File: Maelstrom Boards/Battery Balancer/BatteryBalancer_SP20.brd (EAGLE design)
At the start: 101.6 x 101.6 mm, 83 parts, among them IC3 REG1117, P1 39-30-14?, P2 39-30-16?, Q1 SPB80P06P, Q2 SPB80P06P, Q3 NMOSFET-D2PAK-7, Q4 310mA/60V/1.6Ω, Q5 NMOSFET-D2PAK-7

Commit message: Changed Top Connector Position
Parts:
- removed P1: 39-30-14?, con-molex-mini-fit:39-30-?14?
- added U$4: 14PIN-VERT, Vertical_Connectors:14PIN_VERT
- moved C12 1.20 mm to (31.7, 67.1)
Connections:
- net GND: now also U$4.1-, U$4.2-, U$4.3-, U$4.4-, U$4.5-, U$4.6-, U$4.7-; no longer P1.10, P1.11, P1.12, P1.13, P1.14, P1.8, P1.9
- net MOTOR_POWER: now also U$4.1+, U$4.2+, U$4.3+, U$4.4+, U$4.5+, U$4.6+, U$4.7+; no longer P1.1, P1.2, P1.3, P1.4, P1.5, P1.6, P1.7
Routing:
- net GND: track 94.2 -> 89.0 mm, vias 19 -> 20
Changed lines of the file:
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@@
 <attribute name="VALUE" x="28.742" y="61.668" size="1.27" layer="27"/>
 </element>
-<element name="C12" library="rcl" library_urn="urn:adsk.eagle:library:334" package="E5-10,5" package3d_urn="urn:adsk.eagle:package:23372/1" value="330 uF" x="32.9" y="67.2" smashed="yes">
-<attribute name="NAME" x="37.599" y="69.9432" size="1.27" layer="25" ratio="10"/>
-<attribute name="SPICEPREFIX" value="C" x="31.1" y="18.2" size="1.778" layer="27" display="off"/>
-<attribute name="VALUE" x="29.7758" y="63.9742" size="1.27" layer="27" ratio="10"/>
+<element name="C12" library="rcl" library_urn="urn:adsk.eagle:library:334" package="E5-10,5" package3d_urn="urn:adsk.eagle:package:23372/1" value="330 uF" x="31.7" y="67.1" smashed="yes">
+<attribute name="NAME" x="36.399" y="69.8432" size="1.27" layer="25" ratio="10"/>
+<attribute name="SPICEPREFIX" value="C" x="29.9" y="18.1" size="1.778" layer="27" display="off"/>
+<attribute name="VALUE" x="28.5758" y="63.8742" size="1.27" layer="27" ratio="10"/>
 </element>
 <element name="R24" library="rcl" library_urn="urn:adsk.eagle:library:334" package="R0603" package3d_urn="urn:adsk.eagle:package:23555/2" value="90" x="74.2" y="47.9" smashed="yes" rot="R180">
@@
 </element>
 <element name="U$5" library="Vertical_Connectors" package="6PIN_VERT" value="6PIN-VERT" x="75.2" y="33.3" smashed="yes" rot="R270"/>
-<element name="P1" library="con-molex-mini-fit" package="39-30-?14?" value="39-30-14?" x="54.4" y="84.2" smashed="yes" rot="R180">
-<attribute name="NAME" x="70.802" y="97.2541" size="1.016" layer="25" ratio="18" rot="R270"/>
-<attribute name="VALUE" x="37.528" y="97.5541" size="1.016" layer="27" ratio="10" rot="R270"/>
-</element>
+<element name="U$4" library="Vertical_Connectors" package="14PIN_VERT" value="14PIN-VERT" x="40" y="74.7" smashed="yes" rot="R270"/>
 </elements>
 <signals>
@@
 <contactref element="C7" pad="2"/>
 <wire x1="15.6838" y1="54.635" x2="15.6838" y2="55.905" width="0.1524" layer="1"/>
-<contactref element="P1" pad="10"/>
-<contactref element="P1" pad="8"/>
-<contactref element="P1" pad="12"/>
-<contactref element="P1" pad="14"/>
-<contactref element="P1" pad="9"/>
-<contactref element="P1" pad="11"/>
-<contactref element="P1" pad="13"/>
 <wire x1="15.6838" y1="55.905" x2="15.7" y2="55.9212" width="0.1524" layer="1"/>
 <wire x1="15.7" y1="55.9212" x2="15.7" y2="57.2" width="0.1524" layer="1"/>
@@
 <wire x1="89.4" y1="63.2" x2="89.65" y2="63.45" width="0.1524" layer="1"/>
 <wire x1="91.4" y1="63.45" x2="92.3" y2="62.55" width="0.1524" layer="1"/>
-<wire x1="68.9326" y1="76.7286" x2="66.973" y2="78.6882" width="0.1524" layer="1"/>
-<wire x1="72.4" y1="75.2" x2="70.8714" y2="76.7286" width="0.1524" layer="1"/>
-<wire x1="70.8714" y1="76.7286" x2="68.9326" y2="76.7286" width="0.1524" layer="1"/>
+<contactref element="U$4" pad="7-"/>
+<contactref element="U$4" pad="1-"/>
+<contactref element="U$4" pad="2-"/>
+<contactref element="U$4" pad="3-"/>
+<contactref element="U$4" pad="4-"/>
+<contactref element="U$4" pad="5-"/>
+<contactref element="U$4" pad="6-"/>
+<wire x1="72.4" y1="75.2" x2="72.4" y2="76.9" width="0.1524" layer="1"/>
+<via x="72.4" y="76.9" extent="1-16" drill="0.35"/>
 </signal>
 <signal name="+5V">
@@
 <contactref element="Q1" pad="3"/>
 <contactref element="Q2" pad="3"/>
-<contactref element="P1" pad="1"/>
-<contactref element="P1" pad="3"/>
-<contactref element="P1" pad="5"/>
-<contactref element="P1" pad="7"/>
-<contactref element="P1" pad="4"/>
-<contactref element="P1" pad="6"/>
-<contactref element="P1" pad="2"/>
+<contactref element="U$4" pad="7+"/>
+<contactref element="U$4" pad="1+"/>
+<contactref element="U$4" pad="2+"/>
+<contactref element="U$4" pad="3+"/>
+<contactref element="U$4" pad="4+"/>
+<contactref element="U$4" pad="5+"/>
+<contactref element="U$4" pad="6+"/>
 <polygon width="0.1524" layer="1" thermals="no">
-<vertex x="1.5" y="94"/>
-<vertex x="7.5" y="100"/>
-<vertex x="35.4" y="100"/>
-<vertex x="37.9" y="97.5"/>
-<vertex x="37.9" y="91.3"/>
-<vertex x="40.3" y="88.9"/>
-<vertex x="68" y="88.9"/>
-<vertex x="69.5" y="87.4"/>
-<vertex x="69.5" y="82"/>
-<vertex x="68.3" y="80.8"/>
-<vertex x="28.8" y="80.8"/>
-<vertex x="24.8" y="84.8"/>
-<vertex x="4" y="84.8"/>
-<vertex x="1.5" y="87.3"/>
+<vertex x="24.3" y="84.2"/>
+<vertex x="2.5" y="84.2"/>
+<vertex x="0.6" y="86.1"/>
+<vertex x="0.6" y="98.7"/>
+<vertex x="3.1" y="101.2"/>
+<vertex x="44.3" y="101.2"/>
+<vertex x="68" y="77.5"/>
+<vertex x="68" y="71.9"/>
+<vertex x="66.7" y="70.6"/>
+<vertex x="37.9" y="70.6"/>
 </polygon>
 </signal>
@@
 <contactref element="C12" pad="+"/>
 <contactref element="12VCONVERTER" pad="1,VIN(+)"/>
-<wire x1="30.36" y1="67.2" x2="34.583" y2="62.977" width="0.1524" layer="1"/>
-<wire x1="34.583" y1="62.977" x2="34.583" y2="58.7" width="0.1524" layer="1"/>
+<wire x1="29.16" y1="67.1" x2="34.583" y2="61.677" width="0.1524" layer="1"/>
+<wire x1="34.583" y1="61.677" x2="34.583" y2="58.7" width="0.1524" layer="1"/>
 <wire x1="41.5" y1="62" x2="38.2" y2="58.7" width="0.1524" layer="1"/>
 <wire x1="38.2" y1="58.7" x2="34.583" y2="58.7" width="0.1524" layer="1"/>

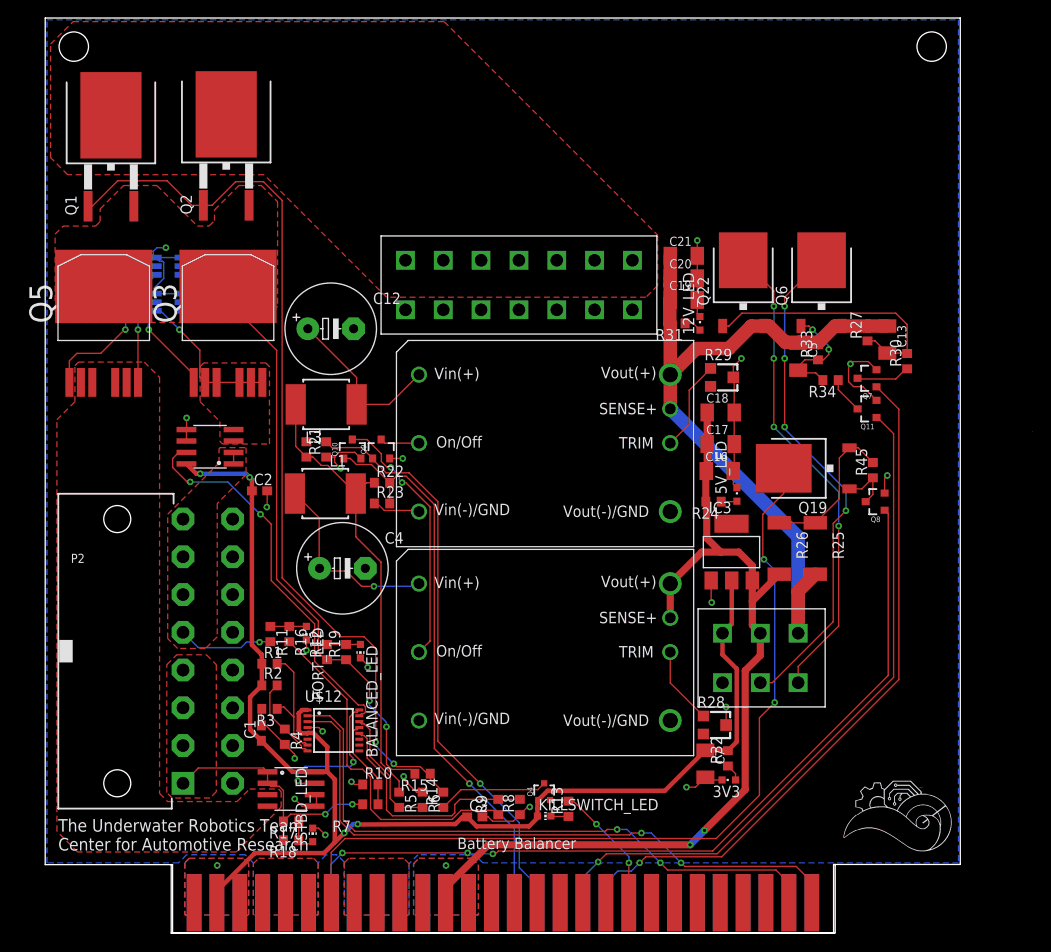
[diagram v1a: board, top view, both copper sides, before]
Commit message: Added connector to BB
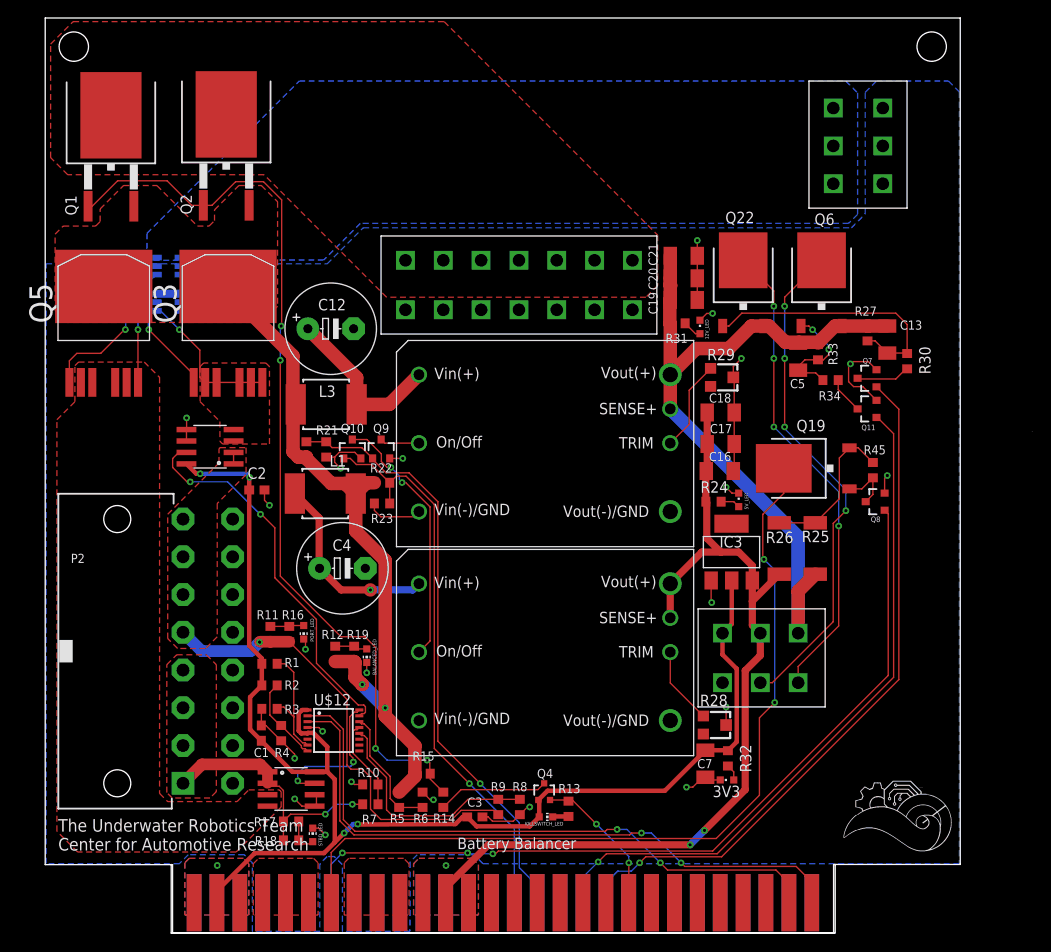
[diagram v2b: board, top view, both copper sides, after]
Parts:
- added U$13: 6PIN-VERT, Vertical_Connectors:6PIN_VERT
- moved R12 0.92 mm to (32.2, 31.0)
- moved R19 0.92 mm to (34.3, 31.0)
- moved BALANCED_LED 0.86 mm to (35.7, 30.8)
- moved 5V_LED 0.63 mm to (77.0, 48.1)
- moved R4 0.57 mm to (26.2, 22.2)
- moved 12V_LED 0.40 mm to (72.7, 67.3)
- moved C2 0.32 mm to (23.5, 49.2)
- moved PORT_LED 0.32 mm to (28.7, 33.4)
- moved KILLSWITCH_LED 0.22 mm to (55.6, 12.9)
- moved 3V3 0.20 mm to (75.7, 17.0)
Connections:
- removed net V+: L1.1, L3.1, R20.1, R22.1, R5.1
- net BALANCED_OUT: now also L1.1, L3.1, R20.1, R22.1, R5.1, U$13.1+, U$13.2+, U$13.3+
- net GND: now also U$13.1-, U$13.2-, U$13.3-
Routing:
- net V+: track 51.2 -> 0.00 mm
- net BALANCED_OUT: track 82.1 -> 90.5 mm, vias 3 -> 2
- net GND: track 89.0 -> 87.6 mm, vias 20 -> 22
- net N$8: track 102.2 -> 103.2 mm, vias 2 -> 4
- net N$10: track 26.3 -> 25.8 mm
- added copper zone on layer 16, net BALANCED_OUT
